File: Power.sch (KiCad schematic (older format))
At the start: 64 parts, among them Q10 AOD514, Q11 AOD514, Q4 2N7002, Q5 2N7002, Q6 2N7002, Q7 ULN2003APWR, Q8 ULN2003APWR, Q9 AOD417, U2 PCF8575

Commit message: TODO: learn to write good commit messages
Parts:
- added C110, C112: 1u, IPC7351-Nominal:CAPC1005X55, symbol C-0402
- added C111, C113, C114: 10u, IPC7351-Nominal:CAPC1608X55, symbol C-0603
- added U6: RT9026GFP, IPC7351-Nominal:SOP50P490X110-11, symbol RT9026GFP
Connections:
- net labels added: EN_V75, EN_V75REF, PV75_SDRAM_VREF, PV75_SDRAM_VTT
- wire segments 289 -> 324

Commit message: Rearrange power control circuit
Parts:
- removed Q4, Q5, Q6: 2N7002, smd-semi:SOT-23, symbol 2N7002
- added Q4, Q5, Q6: FK3303010L, manuf:PANASONIC-SSSMini3-F2-B, symbol FK3303010L
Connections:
- wire segments 324 -> 333
- no-connect marks 2 -> 1
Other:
- moved on the sheet: C82, R59, R60, R61, R62, R63, R64, R65, R66, R67, R69, R70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

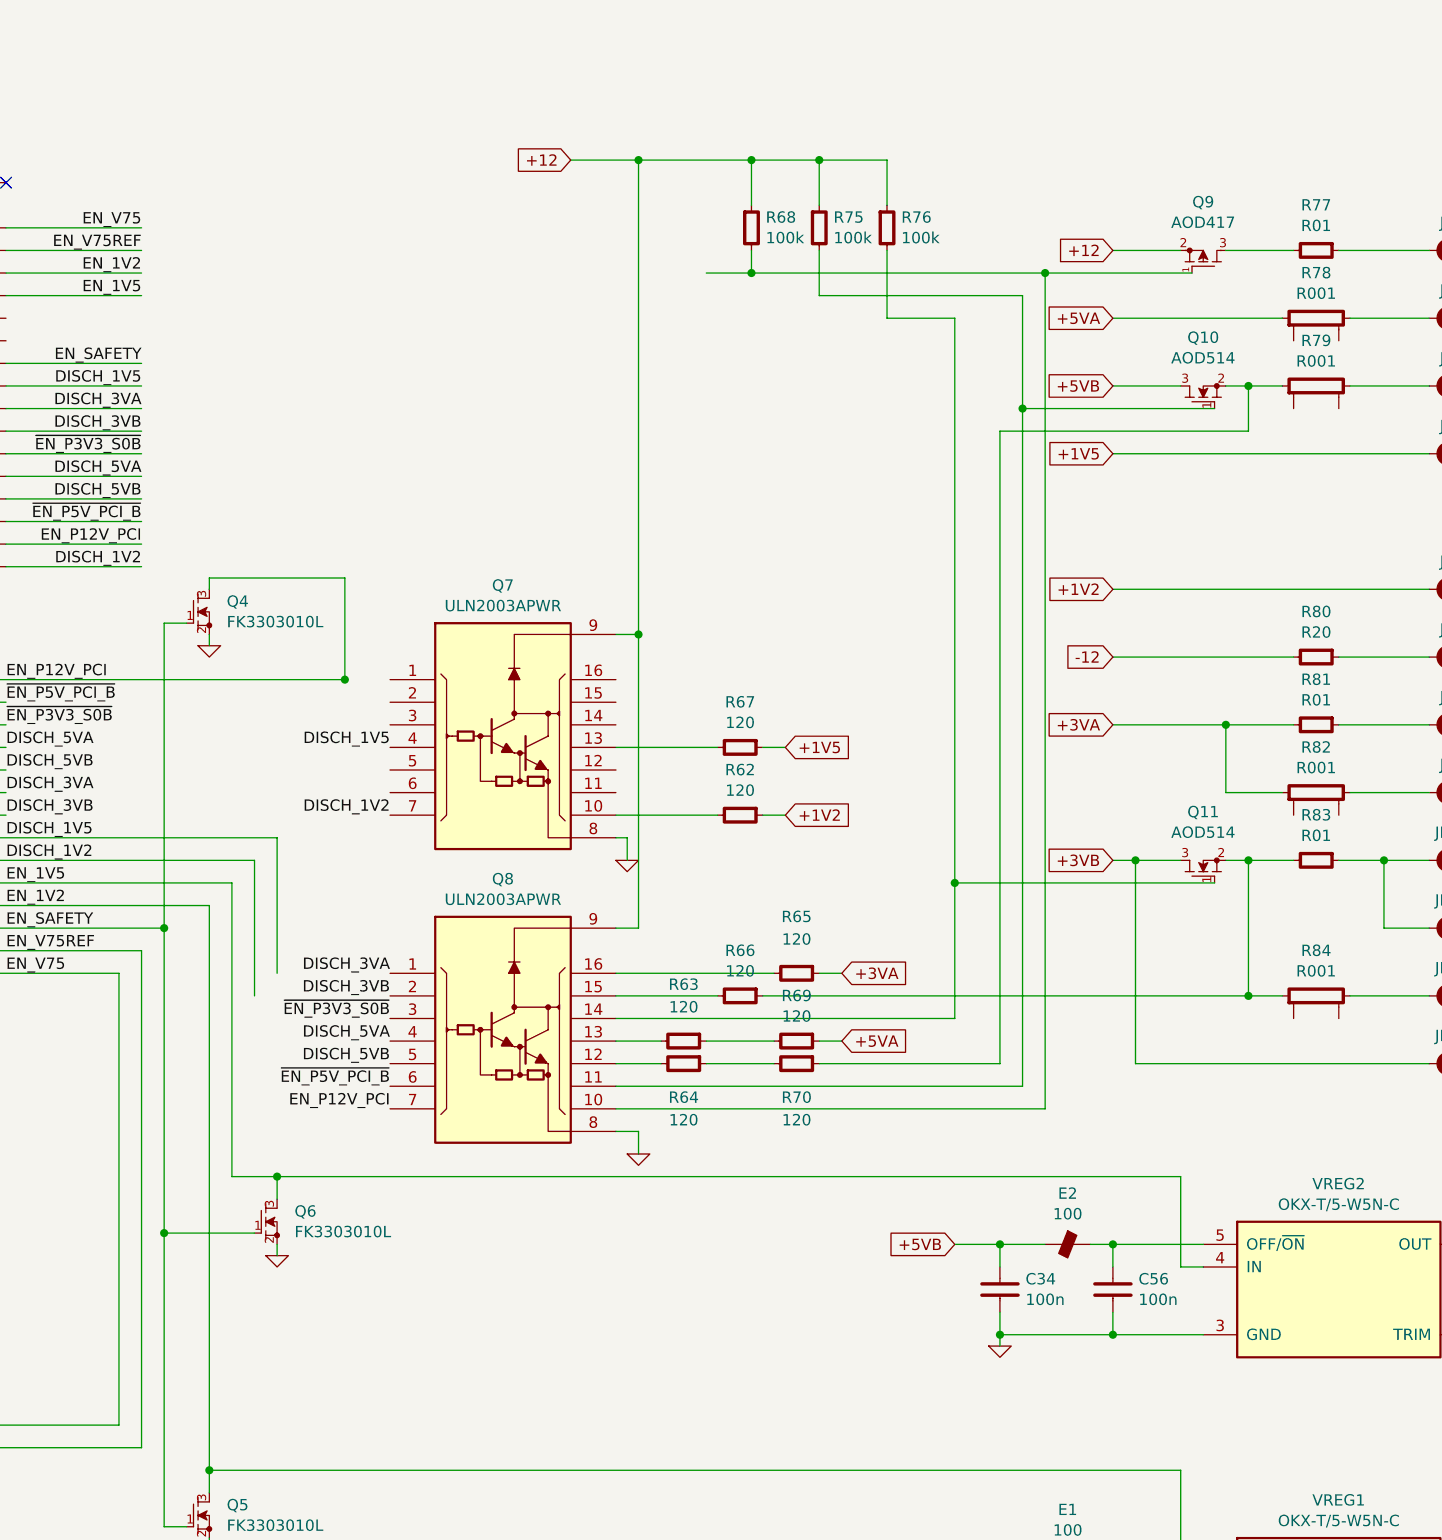
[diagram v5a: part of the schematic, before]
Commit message: Replace ULN2003 with FETs
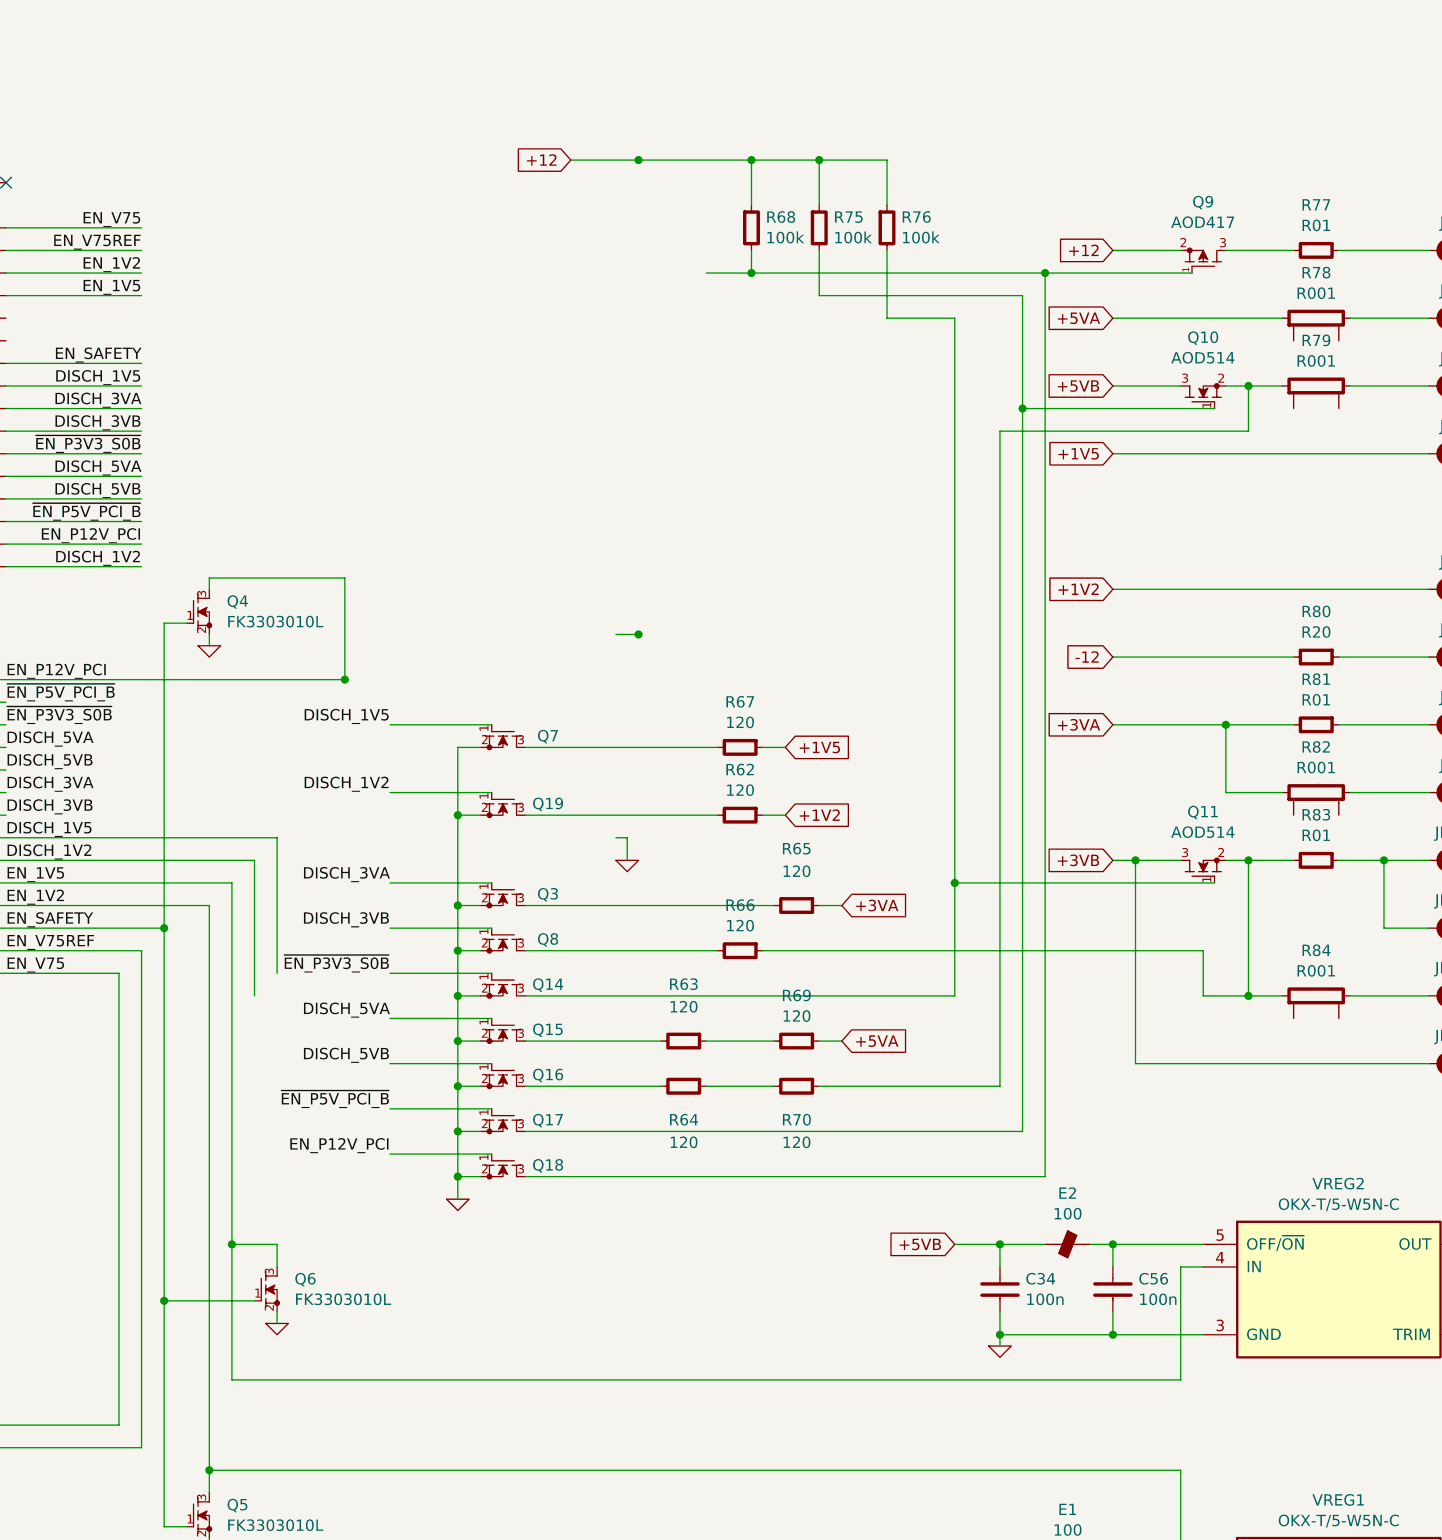
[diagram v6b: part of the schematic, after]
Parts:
- removed Q7, Q8: ULN2003APWR, IPC7351-Nominal:SOP65P640X120-16, symbol ULN2003APWR
- added Q14, Q15, Q16, Q17, Q18, Q19, Q3, Q7, Q8: FK3303010L, manuf:PANASONIC-SSSMini3-F2-B, symbol FK3303010L
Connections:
- wire segments 333 -> 351
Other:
- moved on the sheet: Q6, R64, R65, R66, R70

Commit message: Tidy up page Power
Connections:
- wire segments 351 -> 446
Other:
- moved on the sheet: C110, C111, C112, C113, C114, C3, C33, C34, C4, C5, C55, C56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
